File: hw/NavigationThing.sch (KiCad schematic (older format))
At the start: 32 parts, among them P1 CONN_01X02, SW1 SW_PUSH, U1 HMC5983_module, U2 arduino_nano, U3 PIEZO, U4 NEO-6M_module

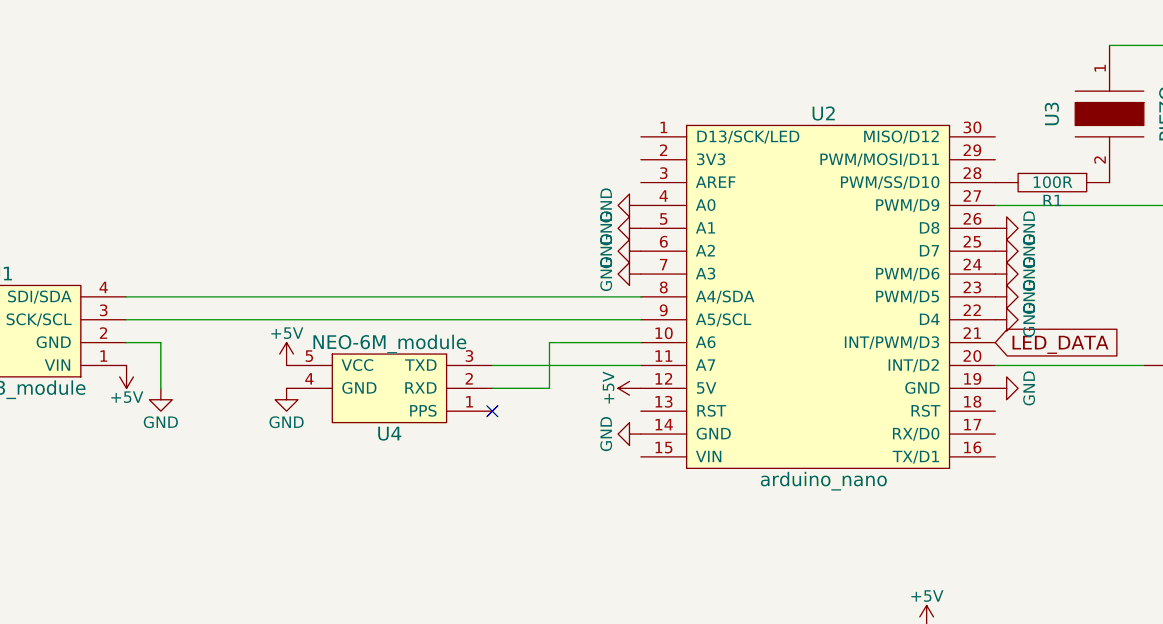
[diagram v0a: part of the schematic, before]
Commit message: New board version
- change GPS pins, as the original ones were purely ADC
- move piezo a little bit to make space for GPS antenna
- add hole for GPS antenna
- change signature to text instead of logo (which does not render in SVG)
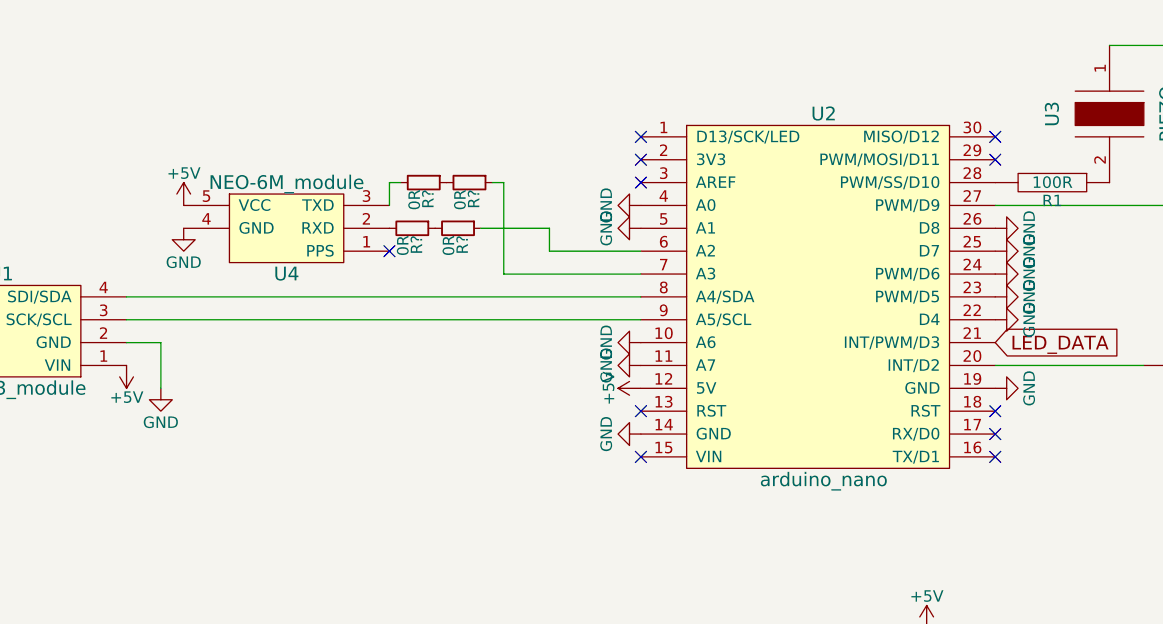
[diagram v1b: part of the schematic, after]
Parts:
- added R? (x4): 0R, symbol R_Small
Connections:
- net GND: now also U2.10 (A6), U2.11 (A7); no longer U2.6 (A2), U2.7 (A3)
- net at U4.2 (RXD): now also R?.2; no longer U2.10 (A6)
- net at U4.3 (TXD): now also R?.2; no longer U2.11 (A7)
- new net: R?.1, U2.6 (A2)
- new net: R?.1, U2.7 (A3)
- new net: R?.1, R?.2 (x2)
- no-connect marks 5 -> 15
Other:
- moved on the sheet: U4
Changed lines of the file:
@@
 L NEO-6M_module U4
 U 1 1 57CBF6BE
-P 3000 3000
-F 0 "U4" H 3000 2800 60  0000 C CNN
-F 1 "NEO-6M_module" H 3000 3200 60  0000 C CNN
-F 2 "yaqwsx:NEO-6M_module" H 3050 2850 60  0001 C CNN
-F 3 "" H 3050 2850 60  0000 C CNN
-	1    3000 3000
+P 2550 2300
+F 0 "U4" H 2550 2100 60  0000 C CNN
+F 1 "NEO-6M_module" H 2550 2500 60  0000 C CNN
+F 2 "yaqwsx:NEO-6M_module" H 2600 2150 60  0001 C CNN
+F 3 "" H 2600 2150 60  0000 C CNN
+	1    2550 2300
 	1    0    0    -1
 $EndComp
@@
 L +5V #PWR030
 U 1 1 57CC2EAA
-P 2550 2900
-F 0 "#PWR030" H 2550 2750 50  0001 C CNN
-F 1 "+5V" H 2550 3040 50  0000 C CNN
-F 2 "" H 2550 2900 50  0000 C CNN
-F 3 "" H 2550 2900 50  0000 C CNN
-	1    2550 2900
+P 2100 2200
+F 0 "#PWR030" H 2100 2050 50  0001 C CNN
+F 1 "+5V" H 2100 2340 50  0000 C CNN
+F 2 "" H 2100 2200 50  0000 C CNN
+F 3 "" H 2100 2200 50  0000 C CNN
+	1    2100 2200
 	1    0    0    -1
 $EndComp
@@
 L GND #PWR031
 U 1 1 57CC2EF9
-P 2550 3000
-F 0 "#PWR031" H 2550 2750 50  0001 C CNN
-F 1 "GND" H 2550 2850 50  0000 C CNN
-F 2 "" H 2550 3000 50  0000 C CNN
-F 3 "" H 2550 3000 50  0000 C CNN
-	1    2550 3000
-	1    0    0    -1
-$EndComp
-NoConn ~ 3450 3100
+P 2100 2300
+F 0 "#PWR031" H 2100 2050 50  0001 C CNN
+F 1 "GND" H 2100 2150 50  0000 C CNN
+F 2 "" H 2100 2300 50  0000 C CNN
+F 3 "" H 2100 2300 50  0000 C CNN
+	1    2100 2300
+	1    0    0    -1
+$EndComp
+NoConn ~ 3000 2400
 $Comp
 L SW_PUSH SW1
@@
 	6850 4350 6850 4300
 Connection ~ 6600 4350
-Wire Wire Line
-	4100 2900 3450 2900
-Wire Wire Line
-	4100 2800 3700 2800
-Wire Wire Line
-	3700 2800 3700 3000
-Wire Wire Line
-	3700 3000 3450 3000
 $Comp
 L GND #PWR037
@@
 $Comp
 L GND #PWR039
-U 1 1 57CC39C9
-P 4100 2400
-F 0 "#PWR039" H 4100 2150 50  0001 C CNN
-F 1 "GND" H 4100 2250 50  0000 C CNN
-F 2 "" H 4100 2400 50  0000 C CNN
-F 3 "" H 4100 2400 50  0000 C CNN
-	1    4100 2400
-	0    1    1    0
-$EndComp
-$Comp
-L GND #PWR040
-U 1 1 57CC3A34
-P 4100 2500
-F 0 "#PWR040" H 4100 2250 50  0001 C CNN
-F 1 "GND" H 4100 2350 50  0000 C CNN
-F 2 "" H 4100 2500 50  0000 C CNN
-F 3 "" H 4100 2500 50  0000 C CNN
-	1    4100 2500
-	0    1    1    0
-$EndComp
-$Comp
-L GND #PWR041
 U 1 1 57CC3A9F
 P 5650 2300
-F 0 "#PWR041" H 5650 2050 50  0001 C CNN
+F 0 "#PWR039" H 5650 2050 50  0001 C CNN
 F 1 "GND" H 5650 2150 50  0000 C CNN
 F 2 "" H 5650 2300 50  0000 C CNN
@@
 $EndComp
 $Comp
-L GND #PWR042
+L GND #PWR040
 U 1 1 57CC3B0A
 P 5650 2400
-F 0 "#PWR042" H 5650 2150 50  0001 C CNN
+F 0 "#PWR040" H 5650 2150 50  0001 C CNN
 F 1 "GND" H 5650 2250 50  0000 C CNN
 F 2 "" H 5650 2400 50  0000 C CNN
@@
 $EndComp
 $Comp
-L GND #PWR043
+L GND #PWR041
 U 1 1 57CC3BFF
 P 5650 2500
-F 0 "#PWR043" H 5650 2250 50  0001 C CNN
+F 0 "#PWR041" H 5650 2250 50  0001 C CNN
 F 1 "GND" H 5650 2350 50  0000 C CNN
 F 2 "" H 5650 2500 50  0000 C CNN
@@
 $EndComp
 $Comp
-L GND #PWR044
+L GND #PWR042
 U 1 1 57CC3C6A
 P 5650 2600
-F 0 "#PWR044" H 5650 2350 50  0001 C CNN
+F 0 "#PWR042" H 5650 2350 50  0001 C CNN
 F 1 "GND" H 5650 2450 50  0000 C CNN
 F 2 "" H 5650 2600 50  0000 C CNN
@@
 $EndComp
 $Comp
-L GND #PWR045
+L GND #PWR043
 U 1 1 57CC3CD5
 P 5650 2700
-F 0 "#PWR045" H 5650 2450 50  0001 C CNN
+F 0 "#PWR043" H 5650 2450 50  0001 C CNN
 F 1 "GND" H 5650 2550 50  0000 C CNN
 F 2 "" H 5650 2700 50  0000 C CNN
@@
 Wire Wire Line
 	6300 2900 5650 2900
+NoConn ~ 4100 1900
+NoConn ~ 4100 2000
+NoConn ~ 4100 2100
+NoConn ~ 5650 3100
+NoConn ~ 5650 3200
+NoConn ~ 5650 3300
+Wire Wire Line
+	3500 2500 4100 2500
+Wire Wire Line
+	3700 2300 3700 2400
+Wire Wire Line
+	3700 2400 4100 2400
+$Comp
+L GND #PWR044
+U 1 1 57CD4D40
+P 4100 2800
+F 0 "#PWR044" H 4100 2550 50  0001 C CNN
+F 1 "GND" H 4100 2650 50  0000 C CNN
+F 2 "" H 4100 2800 50  0000 C CNN
+F 3 "" H 4100 2800 50  0000 C CNN
+	1    4100 2800
+	0    1    1    0
+$EndComp
+$Comp
+L GND #PWR045
+U 1 1 57CD4DAB
+P 4100 2900
+F 0 "#PWR045" H 4100 2650 50  0001 C CNN
+F 1 "GND" H 4100 2750 50  0000 C CNN
+F 2 "" H 4100 2900 50  0000 C CNN
+F 3 "" H 4100 2900 50  0000 C CNN
+	1    4100 2900
+	0    1    1    0
+$EndComp
+NoConn ~ 4100 3100
+NoConn ~ 4100 3300
+NoConn ~ 5650 1900
+NoConn ~ 5650 2000
+$Comp
+L R_Small R?
+U 1 1 57CD5674
+P 3350 2100
+F 0 "R?" H 3380 2120 50  0000 L CNN
+F 1 "0R" H 3380 2060 50  0000 L CNN
+F 2 "" H 3350 2100 50  0000 C CNN
+F 3 "" H 3350 2100 50  0000 C CNN
+	1    3350 2100
+	0    1    1    0
+$EndComp
+Wire Wire Line
+	3000 2200 3000 2100
+Wire Wire Line
+	3000 2100 3050 2100
+Wire Wire Line
+	3450 2100 3500 2100
+Wire Wire Line
+	3500 2100 3500 2500
+$Comp
+L R_Small R?
+U 1 1 57CD539C
+P 3150 2100
+F 0 "R?" H 3180 2120 50  0000 L CNN
+F 1 "0R" H 3180 2060 50  0000 L CNN
+F 2 "" H 3150 2100 50  0000 C CNN
+F 3 "" H 3150 2100 50  0000 C CNN
+	1    3150 2100
+	0    1    1    0
+$EndComp
+$Comp
+L R_Small R?
+U 1 1 57CD5871
+P 3100 2300
+F 0 "R?" H 3130 2320 50  0000 L CNN
+F 1 "0R" H 3130 2260 50  0000 L CNN
+F 2 "" H 3100 2300 50  0000 C CNN
+F 3 "" H 3100 2300 50  0000 C CNN
+	1    3100 2300
+	0    1    1    0
+$EndComp
+$Comp
+L R_Small R?
+U 1 1 57CD58F4
+P 3300 2300
+F 0 "R?" H 3330 2320 50  0000 L CNN
+F 1 "0R" H 3330 2260 50  0000 L CNN
+F 2 "" H 3300 2300 50  0000 C CNN
+F 3 "" H 3300 2300 50  0000 C CNN
+	1    3300 2300
+	0    1    1    0
+$EndComp
+Wire Wire Line
+	3400 2300 3700 2300
 $EndSCHEMATC

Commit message: Small board adjustements
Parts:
- R2, R3, R4, R5: renamed from R?; footprint (none) -> Resistors_SMD:R_0603_HandSoldering
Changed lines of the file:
@@
 NoConn ~ 5650 2000
 $Comp
-L R_Small R?
+L R_Small R5
 U 1 1 57CD5674
 P 3350 2100
-F 0 "R?" H 3380 2120 50  0000 L CNN
+F 0 "R5" H 3380 2120 50  0000 L CNN
 F 1 "0R" H 3380 2060 50  0000 L CNN
-F 2 "" H 3350 2100 50  0000 C CNN
+F 2 "Resistors_SMD:R_0603_HandSoldering" H 3350 2100 50  0001 C CNN
 F 3 "" H 3350 2100 50  0000 C CNN
 	1    3350 2100
@@
 	3500 2100 3500 2500
 $Comp
-L R_Small R?
+L R_Small R3
 U 1 1 57CD539C
 P 3150 2100
-F 0 "R?" H 3180 2120 50  0000 L CNN
+F 0 "R3" H 3180 2120 50  0000 L CNN
 F 1 "0R" H 3180 2060 50  0000 L CNN
-F 2 "" H 3150 2100 50  0000 C CNN
+F 2 "Resistors_SMD:R_0603_HandSoldering" H 3150 2100 50  0001 C CNN
 F 3 "" H 3150 2100 50  0000 C CNN
 	1    3150 2100
@@
 $EndComp
 $Comp
-L R_Small R?
+L R_Small R2
 U 1 1 57CD5871
 P 3100 2300
-F 0 "R?" H 3130 2320 50  0000 L CNN
+F 0 "R2" H 3130 2320 50  0000 L CNN
 F 1 "0R" H 3130 2260 50  0000 L CNN
-F 2 "" H 3100 2300 50  0000 C CNN
+F 2 "Resistors_SMD:R_0603_HandSoldering" H 3100 2300 50  0001 C CNN
 F 3 "" H 3100 2300 50  0000 C CNN
 	1    3100 2300
@@
 $EndComp
 $Comp
-L R_Small R?
+L R_Small R4
 U 1 1 57CD58F4
 P 3300 2300
-F 0 "R?" H 3330 2320 50  0000 L CNN
+F 0 "R4" H 3330 2320 50  0000 L CNN
 F 1 "0R" H 3330 2260 50  0000 L CNN
-F 2 "" H 3300 2300 50  0000 C CNN
+F 2 "Resistors_SMD:R_0603_HandSoldering" H 3300 2300 50  0001 C CNN
 F 3 "" H 3300 2300 50  0000 C CNN
 	1    3300 2300
